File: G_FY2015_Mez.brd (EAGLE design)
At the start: 160 x 100 mm, 181 parts, among them IC100 FT232RL, J1 RPI2_GPIO_HOLES, J100 EPL.00.250.NTN, J101 EPL.00.250.NTN, J102 EPL.00.250.NTN, J103 EPL.00.250.NTN, J180 TOKUDEN_SP6, J181 USB Mini-B Connector, J2 SPACEWIRE_MDMMDM9, J300 SHV_PIGTAIL_LAND, J301 SHV_PIGTAIL_LAND, J600_12V IL-4P-S3EN2, J610 2.1MMJACKTHM, U10 LM60, U100 AD9215, U101 AD8138, U102 LM6142, U11 MCP4822-E/SN, U110 AD9215, U111 AD8138, U112 LM6142, U120 AD9215, U121 AD8138, U122 LM6142, U130 AD9215, U131 AD8138, U132 LM6142, U190 SN65LVDS049, U191 GPS_FGPMMOPA6H, U192 LED-5, U300 OPTON_1PA_12, U301 OPTON_1PA_12, U302 2SC1815, U303 2SJ313, U5 MCP3208-CI/SL, U500 LT6106, U510 LT6106, U6 MCP1525TSOT-23-3, U600 PHT12050WAH, U610 PHT12050WAH, U620 LTC1983ES6-3, U7 LM60, U8 LM60, U9 LM60

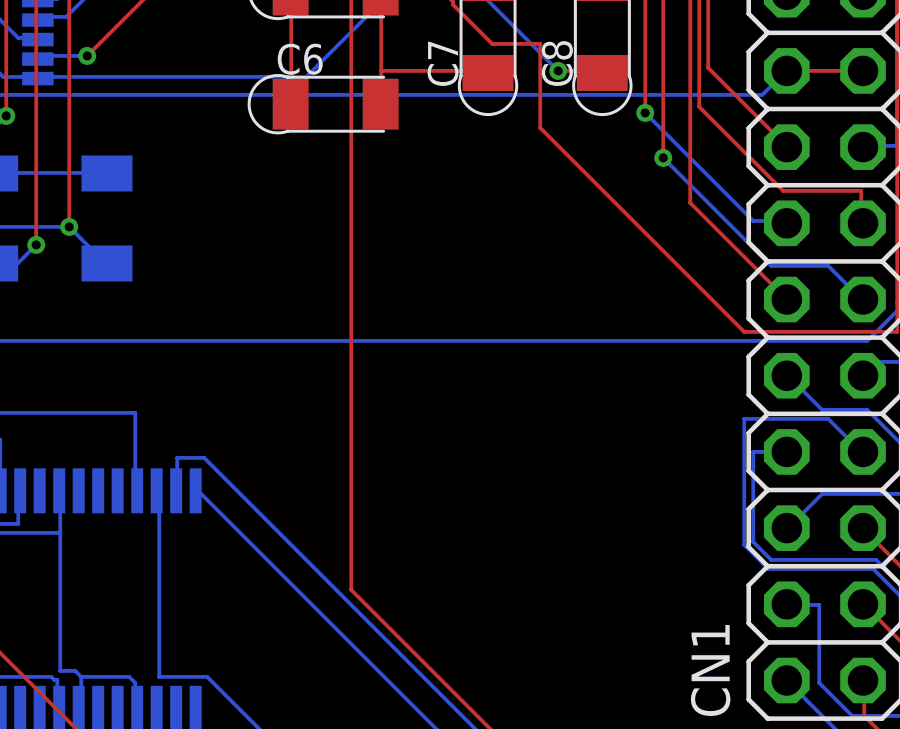
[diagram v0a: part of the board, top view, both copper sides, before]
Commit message: G_FY2015_Mez.brd - GROWTH logo added to the board
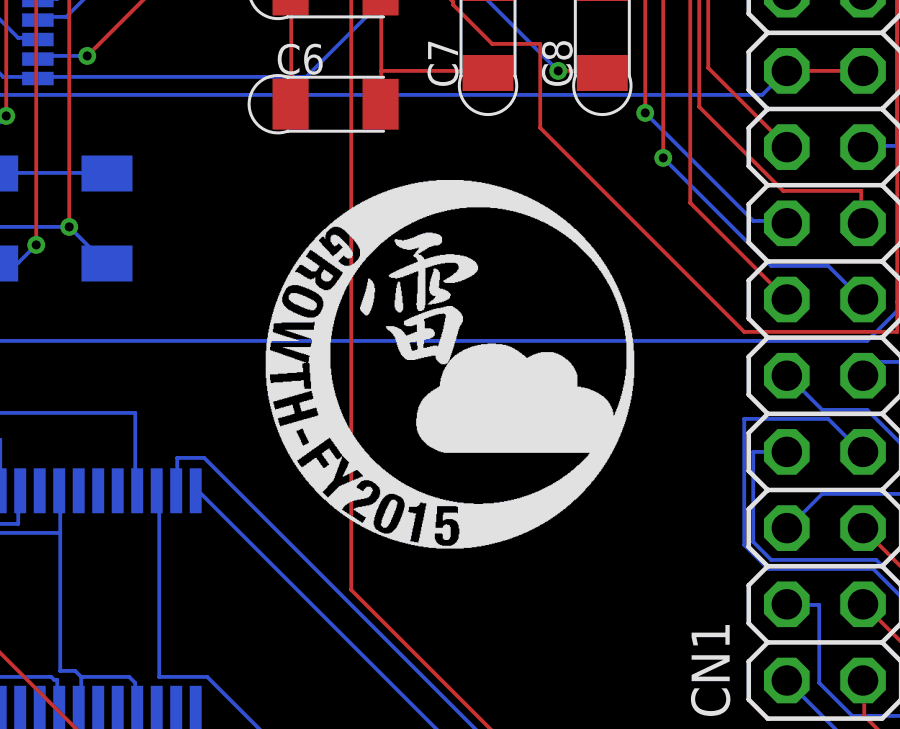
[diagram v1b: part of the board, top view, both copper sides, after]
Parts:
- added U$28: (no value), Aardvark:GROWTH_FY2015_LOGO
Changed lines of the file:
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@@
 </element>
 <element name="U$27" library="Aardvark" package="AARDVARK_LOGO" value="" x="63" y="53.5"/>
+<element name="U$28" library="Aardvark" package="GROWTH_FY2015_LOGO" value="" x="78.96" y="19.488"/>
 </elements>
 <signals>

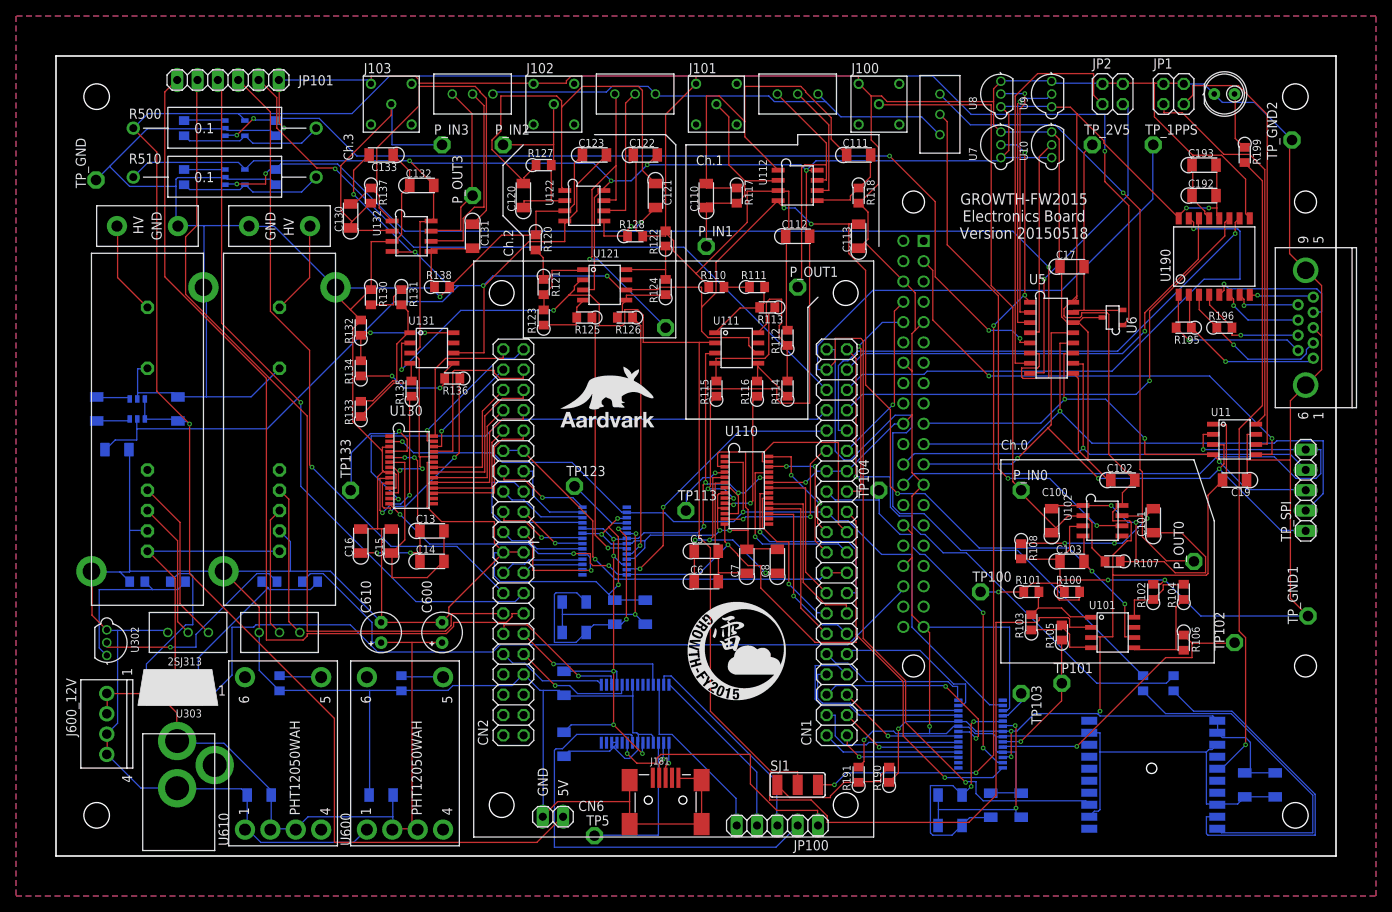
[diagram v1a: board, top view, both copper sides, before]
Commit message: +5V_BEFORE_SENSE and +3V3_BEFORE_SENSE properly connected (previously they were not connected)
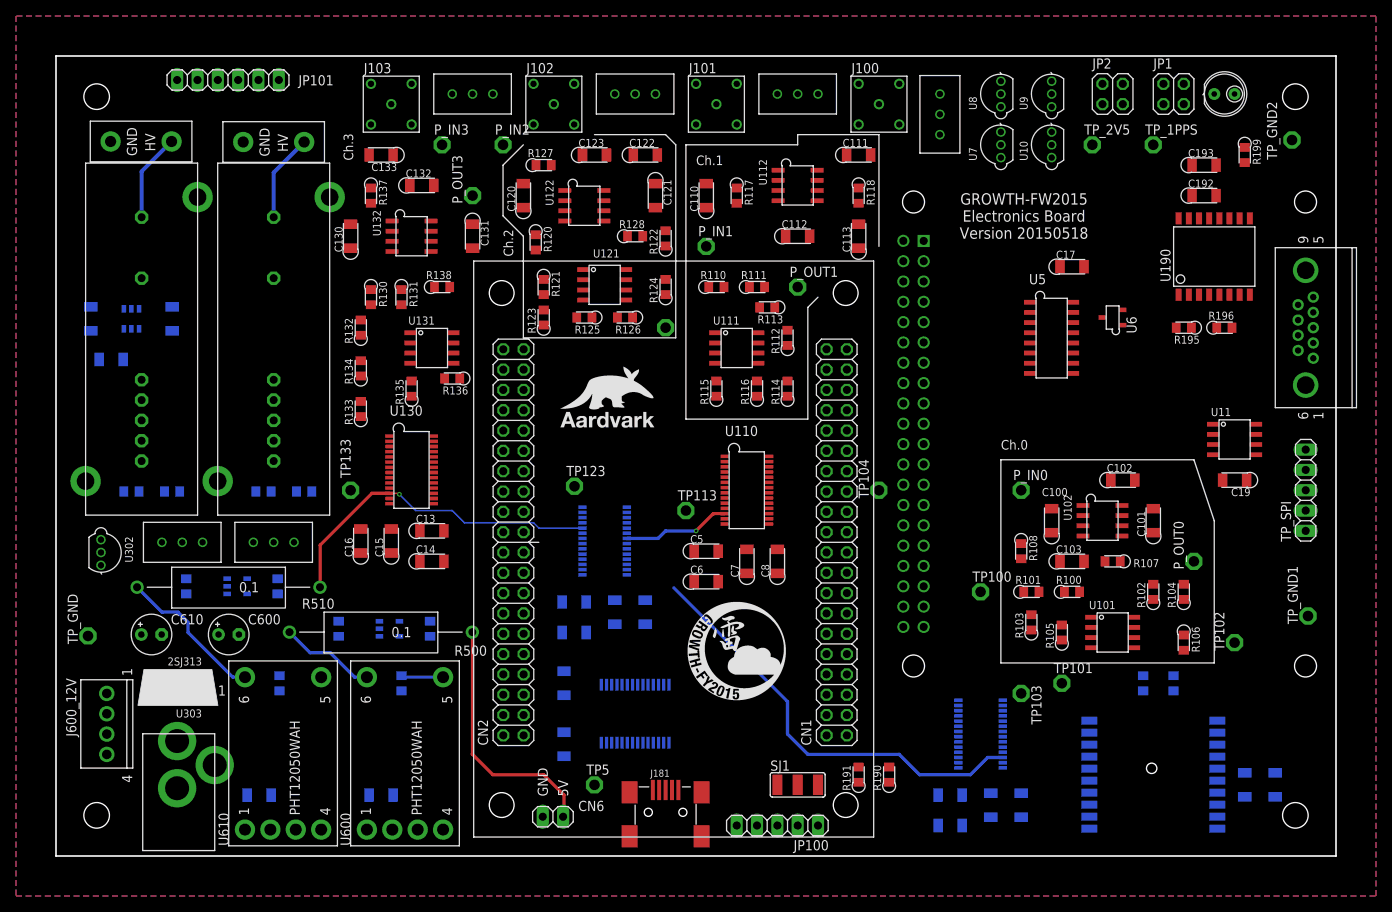
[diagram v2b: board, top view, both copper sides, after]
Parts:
- R302: value 100 -> 4.7k
- moved R500 66.0 mm to (40.6, 28.0), turned to 180 degrees
- moved R501 65.5 mm to (35.3, 28.4)
- moved R502 65.5 mm to (46.8, 28.4)
- moved U500 65.5 mm to (41.7, 28.4)
- moved TP_GND 57.0 mm to (4.00, 27.5)
- moved R510 51.3 mm to (21.6, 33.6), turned to 180 degrees
- moved R511 51.1 mm to (16.3, 33.7)
- moved R512 51.1 mm to (27.7, 33.7)
- moved U510 51.1 mm to (22.6, 33.7)
- moved C610 28.7 mm to (11.9, 27.7), turned to 0 degrees
- moved C600 26.7 mm to (21.6, 27.7), turned to 0 degrees
- moved C620 11.3 mm to (14.5, 67.2)
- moved C621 11.3 mm to (6.89, 62.1)
- moved C622 11.3 mm to (4.35, 67.2)
- moved R300 11.3 mm to (31.0, 45.6)
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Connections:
- removed net 3V3_BEFORE_SENSE: U610.P$6
- removed net 5V_BEFORE_SENSE: U600.P$6
- removed net DIFFAMP0_IN: R100.2, R101.1, TP100.TP
- removed net DIFFAMP1_IN: R110.2, R111.1
- removed net DIFFAMP2_IN: R120.2, R121.1
- removed net DIFFAMP3_IN: R130.2, R131.1
- net +3V3_BEFORE_SENSE: now also U610.P$6
- net +5V_BEFORE_SENSE: now also U600.P$6
- net PREAMP0_OUT: now also R100.2, R101.1, TP100.TP
- net PREAMP1_OUT: now also R110.2, R111.1
- net PREAMP2_OUT: now also R120.2, R121.1
- net PREAMP3_OUT: now also R130.2, R131.1
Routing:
- net GND: track 1355.2 -> 0.00 mm, vias 12 -> 0
- net +3V3: track 578.3 -> 110.1 mm, vias 21 -> 2
- net -3V3: track 274.5 -> 0.00 mm, vias 9 -> 0
- net +5V: track 293.2 -> 31.6 mm, vias 2 -> 0
- net ADC_CM: track 191.4 -> 0.00 mm, vias 2 -> 0
- net GPS_1PPS: track 146.6 -> 0.00 mm, vias 1 -> 0
- net SLOWADC_5: track 133.7 -> 0.00 mm, vias 3 -> 0
- net HV_PWR_ENADIS: track 129.7 -> 0.00 mm
- net ADC_PDWN: track 120.8 -> 0.00 mm, vias 5 -> 0
- net SLOWADC_4: track 119.2 -> 0.00 mm, vias 5 -> 0
- net TRIG_OUT0: track 110.2 -> 0.00 mm
- net +12V: track 105.9 -> 0.00 mm
- net ADC_MODE: track 105.3 -> 0.00 mm, vias 2 -> 0
- net SLOWADC_0: track 105.0 -> 0.00 mm, vias 5 -> 0
- net TRIG_OUT1: track 102.2 -> 0.00 mm
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- added copper zone on layer 16, net GNDBACK
- added copper zone on layer 1, net GNDFRONT
- removed copper zone on layer 1, net GND
- removed copper zone on layer 16, net GND
